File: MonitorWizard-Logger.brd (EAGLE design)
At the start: 120 x 80 mm, 59 parts, among them SW1 ACTION, T1 FDN340P, U1 NCP1117ST50T3G, U2 LP2985-33DBVR, U4-NRF24L01 NRF24L01+-PCB-AERIAL, U5 LMV358IDGKR, U6 ATMEGA328P-PU, U7 RFM69CW, X3 POWERSUPPLY_DC21MMX, Y2 CSTCE16M0V53-R0 16MHZ, Y3 32.768kHz

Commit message: Switch to PNP transistors, connect data lines to chip.
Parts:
- removed T2, T3: (no value), transistor:TO92-CBE
- added Q1, Q2: 2N3906, transistor-pnp:TO92
- added R4, R5, R6, R7, R8, R9: (no value), rcl:0207/10
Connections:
- removed net BTN0: U6.4
- removed net PROC_GND: C12.1, C13.1, ICSP2.6, JP1.P$5, JP1.P$6, PROC_CURRENT.P$1, U6.22, U6.8
- removed net RFMODULE_GND: T2.C, U4-NRF24L01.P$1, U7.14, U7.3
- removed net SENSOR_GND: T3.C
- new net CHIP_SS: R7.1, U6.16
- new net INT0: R9.1, U6.4
- new net N$8: Q2.3, SENSOR_CURRENT.P$2
- net GND: now also C12.1, C13.1, ICSP2.6, JP1.P$5, JP1.P$6, PROC_CURRENT.P$1, U4-NRF24L01.P$1, U6.22, U6.8, U7.14, U7.3; no longer RF_CURRENT.P$2, SENSOR_CURRENT.P$2
- net MISO1: now also R5.1
- net MOSI1: now also R6.1
- net N$2: now also Q1.2, R1.2; no longer RF_CURRENT.P$1, T2.E
- net N$4: now also Q2.2, R3.2; no longer R1.2, T2.B
- net N$5: now also Q1.3, RF_CURRENT.P$2; no longer SENSOR_CURRENT.P$1, T3.E
- net N$6: now also R8.1, U6.12; no longer R3.2, T3.B
- net RFMODULE_CS: now also R7.2
- net RFMODULE_MISC1: now also R8.2
- net RFMODULE_MISC2: now also R9.2
- net RFMODULE_MISO: now also R5.2
- net RFMODULE_MOSI: now also R6.2
- net RFMODULE_POWER_ON: now also U6.14
- net RFMODULE_SCK: now also R4.2
- net SCK1: now also R4.1
- net SENSOR_POWER_ON: now also U6.15
- net VBAT: now also RF_CURRENT.P$1, SENSOR_CURRENT.P$1
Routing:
- removed copper zone on layer 16, net PROC_GND
- removed copper zone on layer 16, net RFMODULE_GND
- removed copper zone on layer 16, net SENSOR_GND

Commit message: Remove redundant components, play with board layout.
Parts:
- removed AD: 6x1F-H8.5, SmartPrj:1X06
- removed C1, C2, C4, C5, C6: 100n, SmartPrj:C0603-ROUND
- removed C3: 1u, SmartPrj:C0603-ROUND
- removed D1: M7, diode:SMB
- removed D2: CD1206-S01575, diode:MINIMELF
- removed ICSP: 3x2 M, SmartPrj:2X03
- removed IOH1: 10x1F-H8.5, SmartPrj:1X10
- removed IOL, POWER: 8x1F-H8.5, SmartPrj:1X08
- removed JP2: 2x2 M - NM, SmartPrj:2X02
- removed L, RX, TX: YELLOW, led:CHIP-LED0805
- removed ON: GREEN, led:CHIP-LED0805
- removed PC1, PC2: 47u, rcl:PANASONIC_D
- removed PROC_CURRENT: CURRENT_MEASURE_0.4A, Probes:CURRENT_MEASURE
- removed R2: 1M, SmartPrj:R0603-ROUND
- removed RESET: TS42031-160R-TR-7260, SmartPrj:TS42
- removed RESET-EN: (no value), jumper:SJ
- removed RN1: 10K, resistor-dil:CAY16
- removed RN2, RN4: 1K, resistor-dil:CAY16
- removed RN3: 22R, resistor-dil:CAY16
- removed T1: FDN340P, zetex:SOT-23
- removed U1: NCP1117ST50T3G, linear:SOT223
- removed U2: LP2985-33DBVR, SmartPrj:SOT23-DBV
- removed U5: LMV358IDGKR, linear:MSOP08
- removed Y2: CSTCE16M0V53-R0 16MHZ, SmartPrj:RESONATOR
- removed ZU4: ATMEGA328P-PU, SmartPrj:DIL28-3
- moved R9 238.5 mm to (74.9, 44.5)
- moved R8 237.1 mm to (74.9, 47.0)
- moved R7 235.6 mm to (74.9, 49.5)
- moved R6 234.3 mm to (74.9, 52.1)
- moved R5 232.9 mm to (74.9, 54.6)
- moved R4 231.5 mm to (74.9, 57.1)
- moved Q2 211.3 mm to (74.9, 10.2), turned to 180 degrees
- moved Q1 198.8 mm to (63.5, 10.2), turned to 180 degrees
- moved U3 148.8 mm to (8.89, 22.9)
- moved SW1 78.2 mm to (16.5, 66.0), turned to 90 degrees
- moved R1 18.0 mm to (59.7, 21.6), turned to 270 degrees
- moved R3 17.6 mm to (71.1, 21.6), turned to 270 degrees
- moved SENSOR_CURRENT 11.4 mm to (76.2, 21.6)
- moved RF_CURRENT 10.2 mm to (64.8, 21.6)
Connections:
- removed net +3V3: C3.2, POWER.4, U2.5, U5.2
- removed net 5-GND: RESET.5
- removed net AD0: AD.1, ZU4.23
- removed net AD1: AD.2, ZU4.24
- removed net AD2: AD.3, ZU4.25
- removed net AD3: AD.4, ZU4.26
- removed net AD4/SDA: AD.5, IOH1.9, ZU4.27
- removed net AD5/SCL: AD.6, IOH1.10, ZU4.28
- removed net CMP: RN1.1, RN1.2, U5.3
- removed net DTR: C5.1, RN2.4
- removed net GATE_CMD: T1.3, U5.1
- removed net IO0: IOL.1, RN4.2, ZU4.2
- removed net IO1: IOL.2, RN4.1, ZU4.3
- removed net IO2: IOL.3, ZU4.4
- removed net IO3: IOL.4, ZU4.5
- removed net IO4: IOL.5, ZU4.6
- removed net IO5: IOL.6, ZU4.11
- removed net IO6: IOL.7, ZU4.12
- removed net IO7: IOL.8, ZU4.13
- removed net IO8: IOH1.1, ZU4.14
- removed net IO9: IOH1.2, ZU4.15
- removed net L13: RN2.8, U5.6, U5.7
- removed net M8RXD: RN4.7
- removed net M8TXD: RN4.8
- removed net MISO: ICSP.1, IOH1.5, ZU4.18
- removed net MOSI: ICSP.4, IOH1.4, ZU4.17
- removed net N$1: L.A, RN2.1
- removed net N$3: ON.A, RN4.5, RN4.6
- removed net N$35: RN2.7, RX.A
- removed net N$36: RN2.6, TX.A
- removed net PB4: JP2.1
- removed net PB5: JP2.3
- removed net PB6: JP2.2
- removed net PB7: JP2.4
- removed net PWRIN: D1.A
- removed net RESET: C5.2, D2.A, ICSP.5, POWER.3, RESET-EN.1, RESET-EN.2, RESET.3, RESET.4, RN1.4, ZU4.1
- removed net RXLED: RX.C
- removed net SCK: ICSP.3, IOH1.6, U5.5, ZU4.19
- removed net SS: IOH1.3, ZU4.16
- removed net TXLED: TX.C
- removed net USBVCC: T1.1
- removed net VIN: D1.C, PC1.+, POWER.8, RN1.8, U1.3
- removed net XTAL1: R2.1, Y2.3, ZU4.9
- removed net XTAL2: R2.2, Y2.1, ZU4.10
- net +5V: no longer C1.2, C2.2, C6.2, D2.C, ICSP.2, PC2.+, POWER.2, POWER.5, RN1.5, RN2.2, RN2.3, RN4.3, RN4.4, T1.2, U1.2, U1.4, U2.1, U2.3, U5.8, ZU4.20, ZU4.7
- net AREF: no longer C4.2, IOH1.8, ZU4.21
- net GND: no longer C1.1, C2.1, C3.1, C4.1, C6.1, ICSP.6, IOH1.7, L.C, ON.C, PC1.-, PC2.-, POWER.6, POWER.7, PROC_CURRENT.P$1, PROC_CURRENT.P$2, RESET.1, RESET.2, RN1.7, RN2.5, U1.1, U2.2, U5.4, Y2.2, ZU4.22, ZU4.8

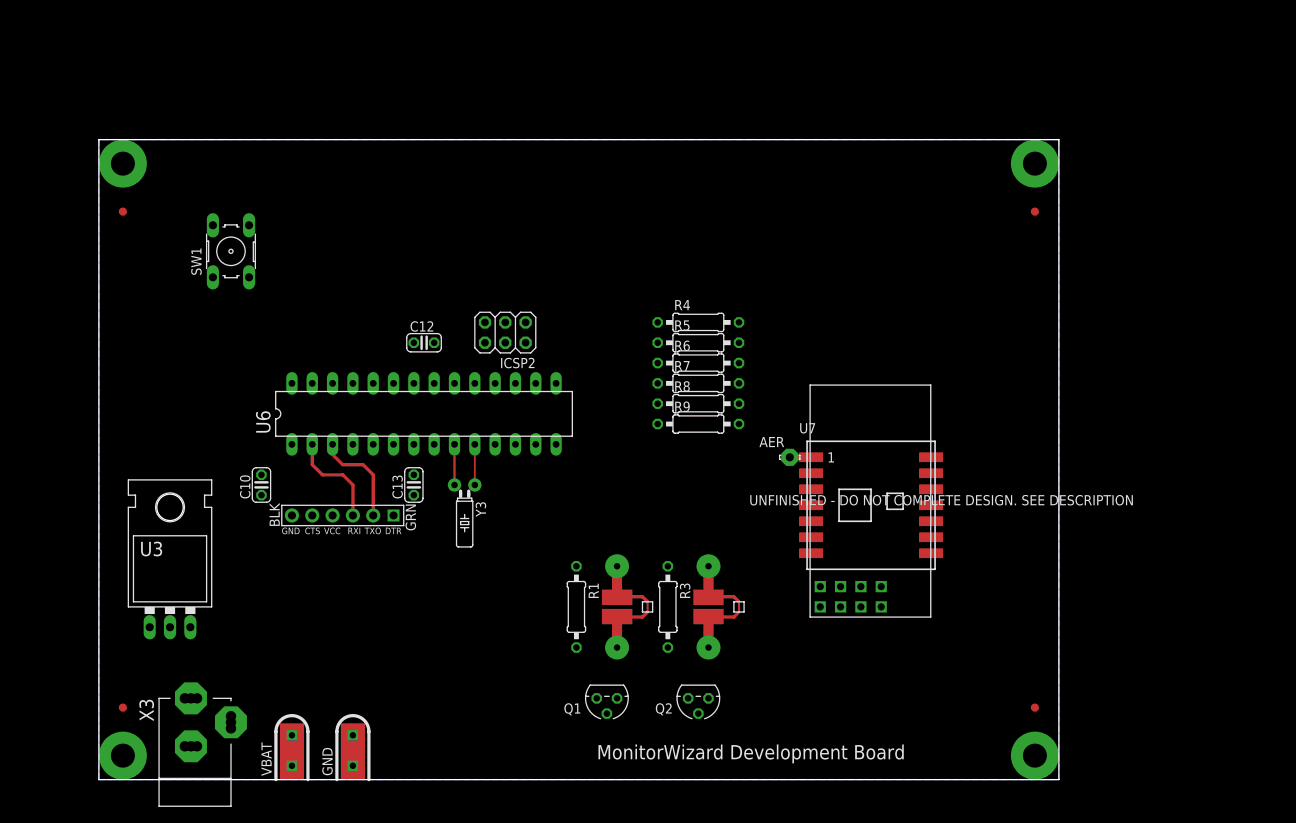
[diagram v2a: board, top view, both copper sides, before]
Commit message: Add DHT22 library, tweak board layout. Still unfinished.
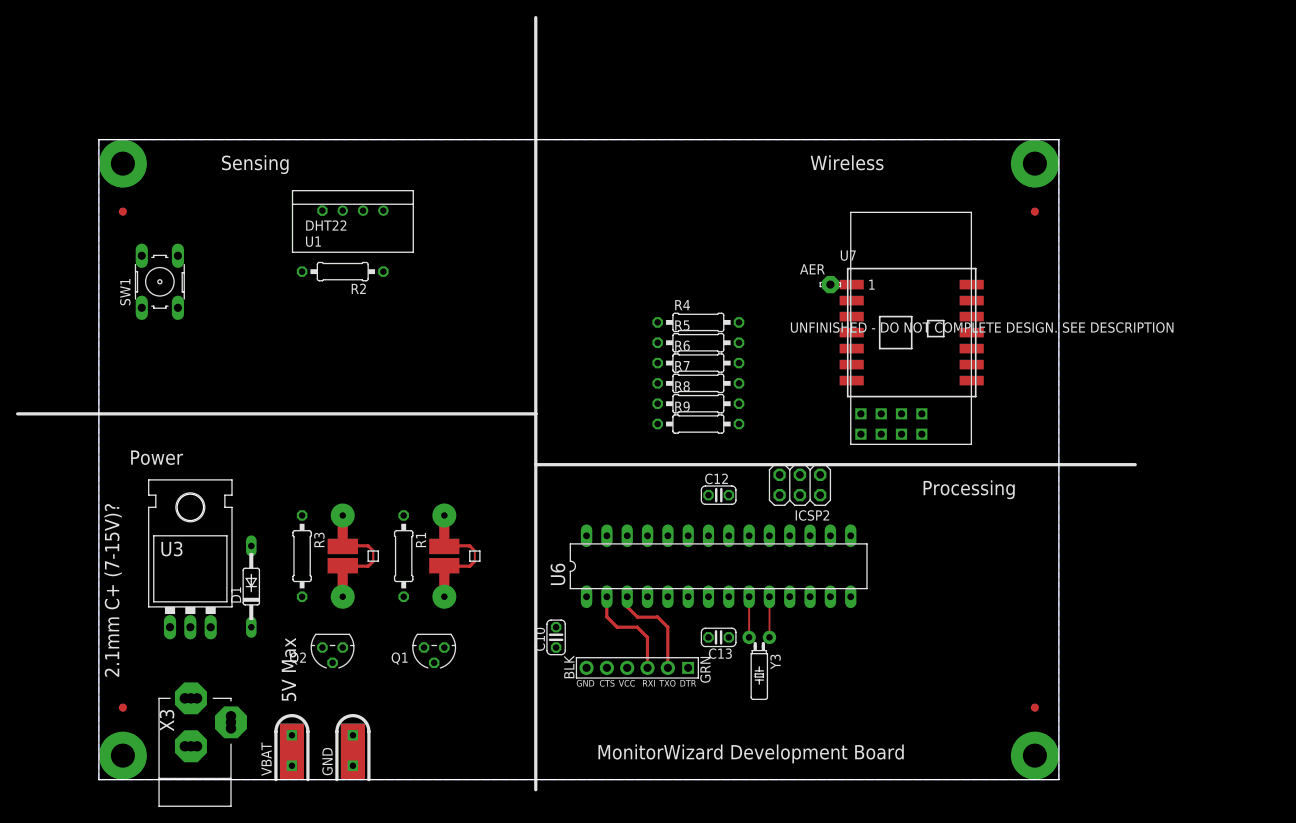
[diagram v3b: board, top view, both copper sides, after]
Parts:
- added D1: 1N4148DO35-10, diode:DO35-10
- added R2: 10K, resistor:0207/10
- added U1: DHT22, RHT03_DHT-22_AM2302:RHT03_DHT-22
- U3: value (none) -> 7805-TO220
- moved Q2 46.2 mm to (29.2, 16.5)
- moved R3 46.2 mm to (25.4, 27.9)
- moved SENSOR_CURRENT 46.2 mm to (30.5, 27.9)
- moved C13 42.6 mm to (77.5, 17.8), turned to 180 degrees
- moved ICSP2 41.5 mm to (87.6, 36.8)
- moved JP1 41.5 mm to (67.3, 14.0)
- moved C10 41.5 mm to (57.1, 17.8)
- moved C12 41.5 mm to (77.5, 35.6)
- moved U6 41.5 mm to (77.5, 26.7)
- moved Y3 41.5 mm to (82.5, 17.8)
- moved Q1 22.5 mm to (41.9, 16.5)
- moved R1 22.5 mm to (38.1, 27.9)
- moved RF_CURRENT 22.5 mm to (43.2, 27.9)
- moved AER 22.2 mm to (91.4, 61.9)
- moved U4-NRF24L01 22.2 mm to (99.1, 44.5)
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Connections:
- removed net N$7: U3.OUT
- new net 5V_REG: D1.A, U3.OUT
- new net DHT22_DATA: R2.1, U1.DATA, U6.23
- new net SENSOR_3V3: R2.2, U1.VDD
- net GND: now also U1.GND
- net VBAT: now also D1.C
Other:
- board text added: "2.1mm C+ (7-15V)?"
- board text added: "5V Max"
- board text added: "Power"
- board text added: "Processing"
- board text added: "Sensing"
- board text added: "Wireless"

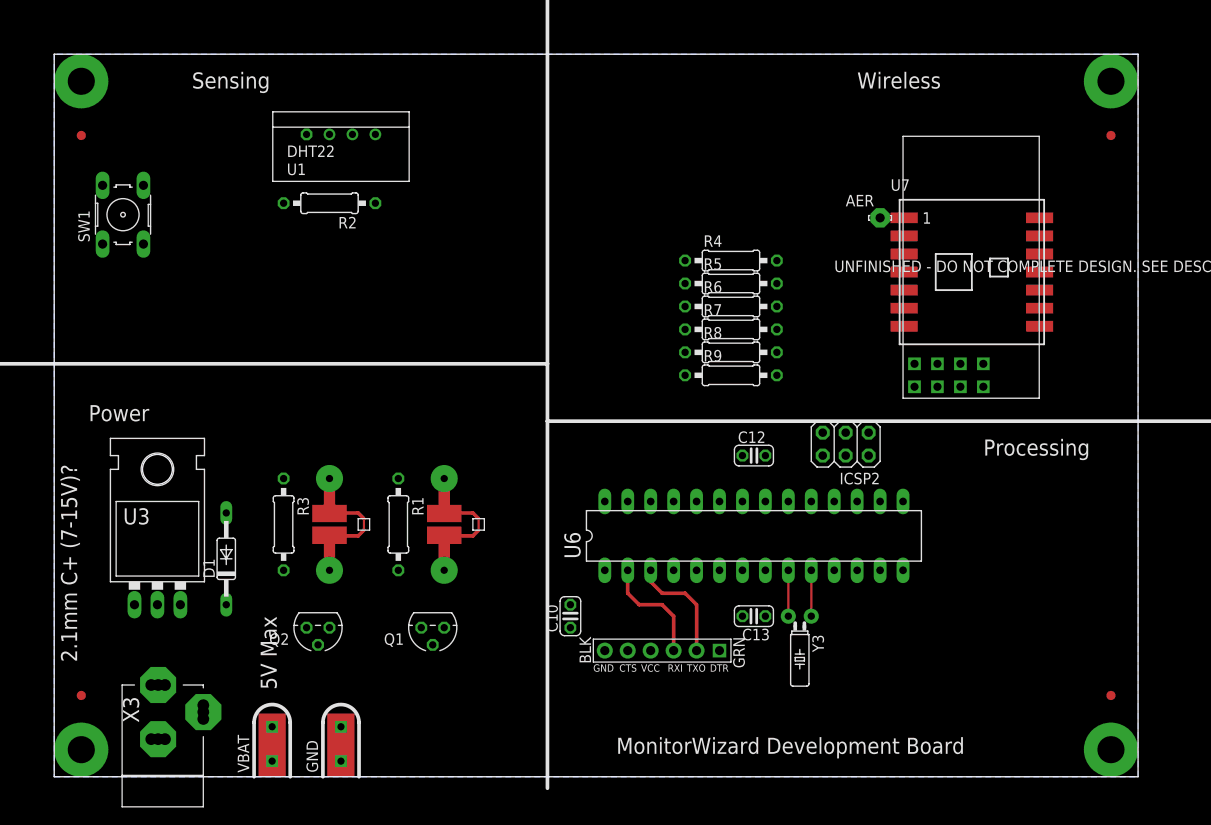
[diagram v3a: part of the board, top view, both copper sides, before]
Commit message: Replace power supply with low power switching setup. Remove resistors for level shifting, since everything will now be running at 3.3v.
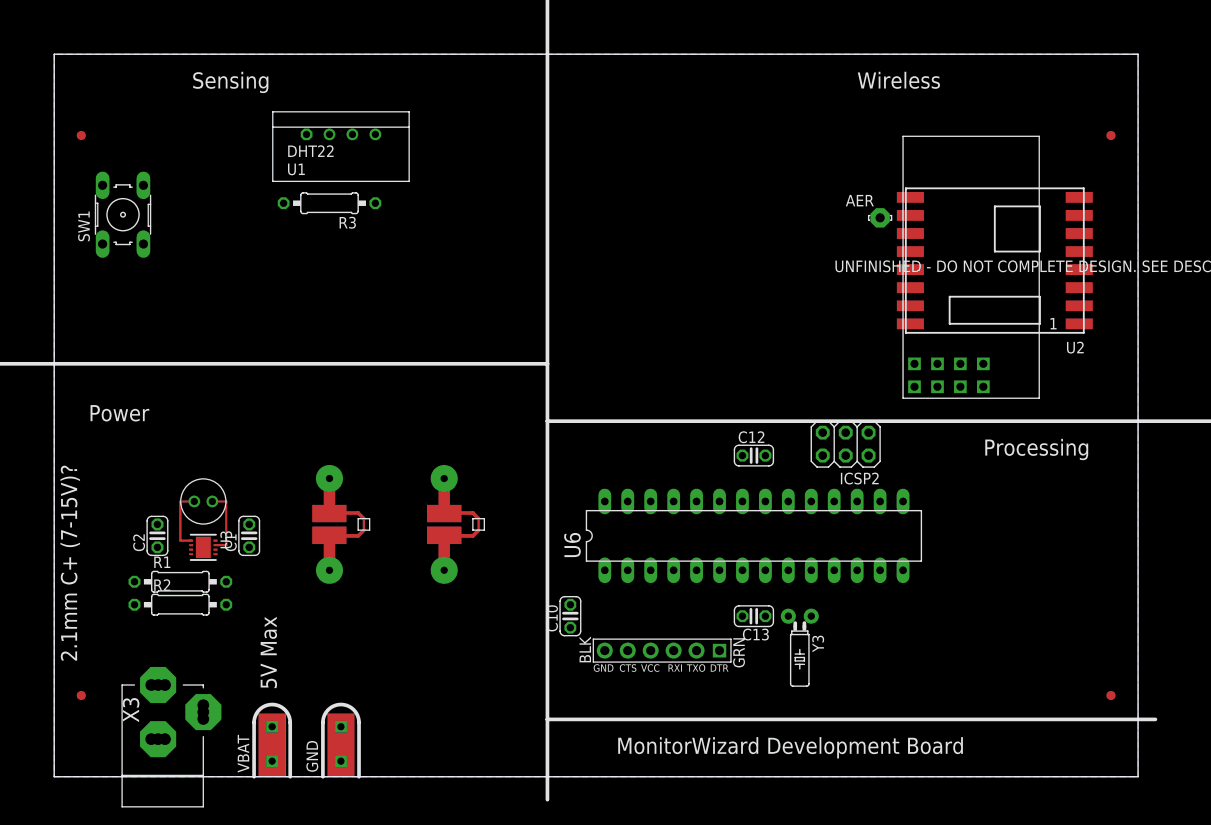
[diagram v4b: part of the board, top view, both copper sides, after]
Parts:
- removed D1: 1N4148DO35-10, diode:DO35-10
- removed Q1, Q2: 2N3906, transistor-pnp:TO92
- removed R4, R5, R6, R7, R8, R9: (no value), rcl:0207/10
- removed U7: RFM69CW, SparkFun-RF:RFM69CW-XXXS2
- added C1: 10uH, rcl:C025-024X044
- added C2: 2.2uH, rcl:C025-024X044
- added L1: 10uH, InductorsThru:L-RADIAL-2-5OD
- added U2: RFM69HW, SparkFun-RF:RFM69W-XXXS2
- R2: value 10K -> (none)
- R3: value (none) -> 10K
- U3: value 7805-TO220 -> LTC3531; device SparkFun-PowerIC:TO-220-ALT -> linear-sen:DFN8-3X3
- moved R2 47.4 mm to (14.0, 19.1), turned to 0 degrees
- moved R3 35.9 mm to (30.5, 63.5), turned to 180 degrees
- moved R1 25.0 mm to (14.0, 21.6), turned to 0 degrees
- moved U3 5.68 mm to (16.5, 25.4), turned to 270 degrees
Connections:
- removed net 5V_REG: D1.A, U3.OUT
- removed net CHIP_SS: R7.1, U6.16
- removed net INT0: R9.1, U6.4
- removed net N$4: Q2.2, R3.2
- removed net N$5: Q1.3, RF_CURRENT.P$2
- removed net N$6: R8.1, U6.12
- removed net N$8: Q2.3, SENSOR_CURRENT.P$2
- removed net RFMODULE_POWER_ON: R1.1, U6.14
- removed net SENSOR_POWER_ON: R3.1, U6.15
- new net 3V3: C1.1, R2.2, RF_CURRENT.P$1, U3.6
- new net N$1: L1.P$2, U3.7
- new net N$3: R1.2, R2.1, U3.5
- new net RF_SS: U6.16
- new net SENSOR_POWER: SENSOR_CURRENT.P$1, U6.15
- net DHT22_DATA: now also R3.1; no longer R2.1
- net GND: now also C1.2, C2.2, R1.1, U2.11, U2.9, U3.3, U3.8, U3.EXP; no longer U3.GND, U7.14, U7.3
- net MISO1: no longer R5.1
- net MOSI1: no longer R6.1
- net N$2: now also L1.P$1, U3.1; no longer Q1.2, R1.2
- net N$9: now also U2.10; no longer U7.1
- net RFMODULE_3V3: now also RF_CURRENT.P$2, U2.8; no longer U7.2
- net RFMODULE_CS: now also U2.15; no longer R7.2, U7.7
- net RFMODULE_MISC1: now also U2.1, U6.12; no longer R8.2, U7.13
- net RFMODULE_MISC2: now also U2.2, U6.4; no longer R9.2, U7.9
- net RFMODULE_MISO: now also U2.13; no longer R5.2, U7.8
- net RFMODULE_MOSI: now also U2.14; no longer R6.2, U7.5
- net RFMODULE_SCK: now also U2.12; no longer R4.2, U7.6
- net SCK1: no longer R4.1
- net SENSOR_3V3: now also R3.2, SENSOR_CURRENT.P$2; no longer R2.2
- net VBAT: now also C2.1, U3.2, U3.4; no longer D1.C, RF_CURRENT.P$1, SENSOR_CURRENT.P$1
- net VBJ: no longer U3.IN
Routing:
- net 328_RXD: track 12.5 -> 0.00 mm
- net 328_TXD: track 12.5 -> 0.00 mm
- net N$1: track 0.00 -> 7.56 mm
- net N$2: track 0.00 -> 7.06 mm
- net XTAL_P: track 5.08 -> 0.00 mm
- net XTAL_N: track 5.08 -> 0.00 mm
- net N$9: track 2.66 -> 0.00 mm
